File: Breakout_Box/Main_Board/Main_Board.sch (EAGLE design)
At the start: 19 parts, among them CN1 19PIN_LEMO

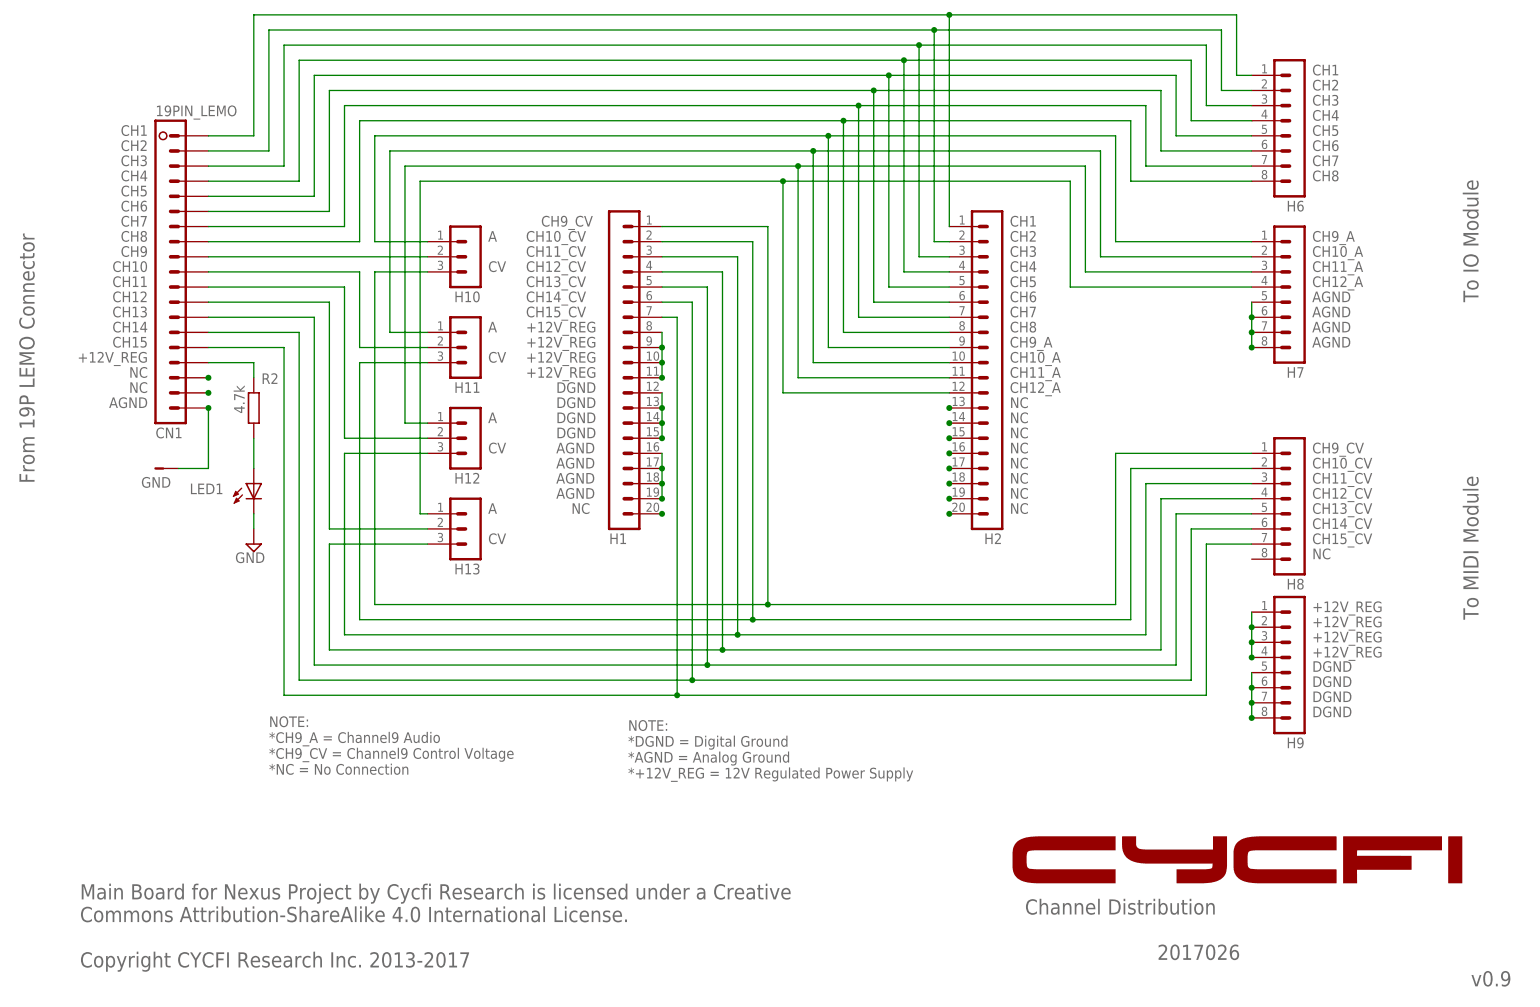
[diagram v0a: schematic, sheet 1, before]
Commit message: Create version_2.0 with updated main and midi modules
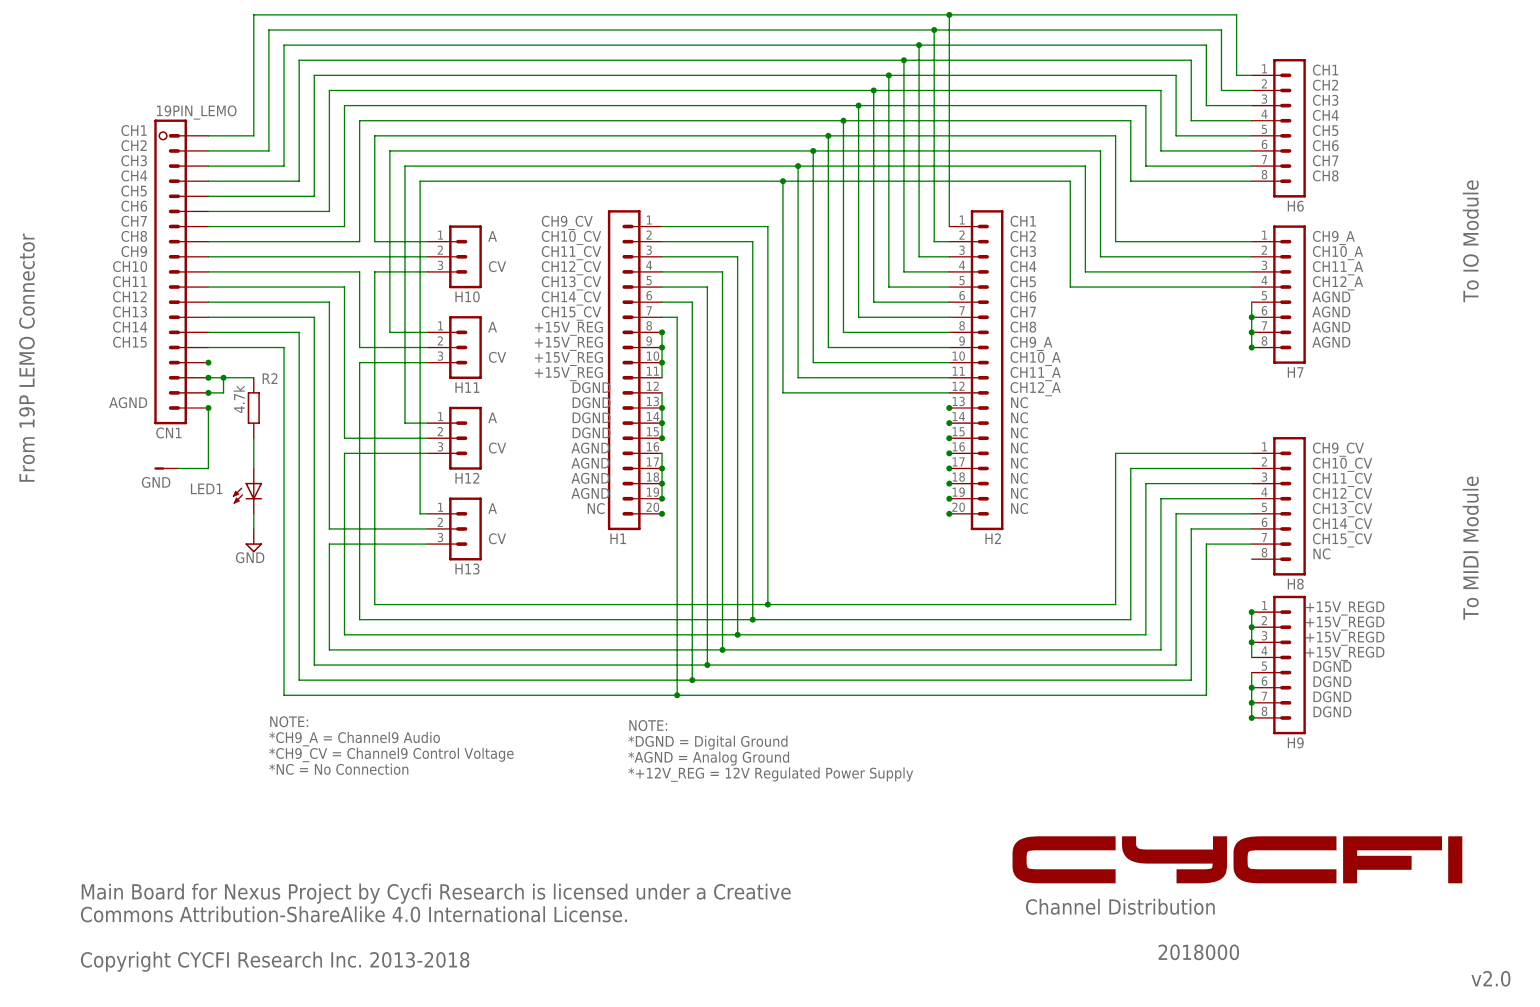
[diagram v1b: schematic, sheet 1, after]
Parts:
- added C1, C3: 22uF, resistor:C-EUC0805
- added L2: 100uH, resistor:L-EU
- L1: value 100uH -> 100mH; device resistor:L-EU -> inductors:SDR
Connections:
- removed net +12V_REG: C2.1, C6.+, CN1.16, H1.10, H1.11, H1.8, H1.9, H9.1, H9.2, H9.3, H9.4, L1.2, R2.1
- removed net N$26: CN1.18
- removed net N$9: CN1.17
- new net +15V_REG: C1.1, C2.1, C6.+, CN1.17, CN1.18, H1.10, H1.11, H1.8, H1.9, L1.1, L2.2, R2.1
- new net +15V_REGD: C3.1, H9.1, H9.2, H9.3, H9.4, L1.2
- new net NC: CN1.16
- net DGND: now also C1.2, C3.2
- net N$31: now also L2.1; no longer L1.1
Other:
- note added: "+15V_REG"
- note added: "2018000"
- note added: "Main Board for Nexus Project by Cycfi Research is licensed under a Creative Commons Attribution-ShareAlike 4.0 International License. Copyright CYCFI Research Inc. 2013-2018"
- note added: "v2.0"
- note removed: "2017026"
- note removed: "Main Board for Nexus Project by Cycfi Research is licensed under a Creative Commons Attribution-ShareAlike 4.0 International License. Copyright CYCFI Research Inc. 2013-2017"
- note removed: "v0.9"
- note removed: "v0.92"
- moved on the sheet: L1
